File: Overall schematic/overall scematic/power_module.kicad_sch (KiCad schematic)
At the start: 0 parts

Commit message: update kicad
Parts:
- added C1, C3: 10uf, Capacitor_SMD:C_0402_1005Metric, symbol Device:C
- added C4: 4.7uf, Capacitor_SMD:C_0402_1005Metric, symbol Device:C
- added C5: 4.7 uf, Capacitor_SMD:C_0402_1005Metric, symbol Device:C
- added D1: Red LED, LED_SMD:LED_0805_2012Metric, symbol Device:LED
- added D2: Zener Diode, Diode_THT:D_DO-34_SOD68_P2.54mm_Vertical_AnodeUp, symbol Diode:1N47xxA
- added D3: Green LED, Diode_SMD:D_0805_2012Metric, symbol Device:LED
- added J1: USB_B_Micro, Connector_USB:USB_Micro-B_Amphenol_10118194_Horizontal, symbol Connector:USB_B_Micro
- added J2: Battery Charger IC TP4056, SOIC127P600X175-9N, symbol TP4056:TP4056
- added J3, J4, J5, J6: Conn_01x02_Pin, Connector_PinHeader_2.54mm:PinHeader_1x02_P2.54mm_Horizontal, symbol Connector:Conn_01x02_Pin
- added J3_Battery1: Conn_01x02, Connector_Pin:Pin_D1.1mm_L10.2mm_W3.5mm_Flat, symbol Connector_Generic:Conn_01x02
- added Q1, Q2: PMOS, Package_TO_SOT_SMD:SOT-23, symbol Simulation_SPICE:PMOS
- added R1, R2: 1k, Resistor_SMD:R_0402_1005Metric, symbol Device:R
- added R10: 1.6k, Resistor_SMD:R_0201_0603Metric, symbol Device:R
- added R3: 3.6M, Resistor_SMD:R_0402_1005Metric, symbol Device:R
- added R4: 3M, Resistor_SMD:R_0402_1005Metric, symbol Device:R
- added R5: 2.5M, Resistor_SMD:R_0402_1005Metric, symbol Device:R
- added R6: 150k, Resistor_SMD:R_0402_1005Metric, symbol Device:R
- added R7: 1M, Resistor_SMD:R_0402_1005Metric, symbol Device:R
- added R8: 10M, Resistor_SMD:R_0402_1005Metric, symbol Device:R
- added R9: 400m, Resistor_SMD:R_0402_1005Metric, symbol Device:R
- added TP1, TP2, TP3, TP4, TP5: TestPoint, symbol Connector:TestPoint
- added U3: Voltage Regulator LM3670MF, Package_TO_SOT_SMD:TSOT-23-5, symbol Regulator_Switching:LM3670MF
- added U4: LM2902, symbol Amplifier_Operational:LM2902
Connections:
- new net: Q1.2 (G), R7.1
- new net: J5.2 (Pin_2), Q1.3 (S), R3.1, R5.1, U4.4 (V+)
- new net: R3.2, R4.1, U4.2 (-)
- new net: D3.1 (K), R1.1
- new net: J2.7 (~{CHRG}), R1.2
- new net: J2.2 (PROG2), R10.1
- new net: C1.1, J2.5 (BAT), J4.1 (Pin_1), TP2.1
- new net: J2.6 (~{STDBY}), R2.2
- new net: D1.1 (K), R2.1
- new net: D2.2 (A), R6.1, R8.2, U4.11 (V-)
- new net: R7.2, R8.1, U4.1
- new net: D2.1 (K), R5.2, U4.3 (+)
- new net: C4.1, J6.2 (Pin_2), U3.1 (Vin), U3.3 (EN)
- new net Data +: J1.3 (D+)
- new net Data -: J1.2 (D-)
- new net GND: C1.2, C3.2, C4.2, C5.2, J1.5 (GND), J1.6 (Shield), J2.1 (TEMP1), J2.3 (GND_3), J2.4 (VCC4), J3_Battery1.2 (Pin_2), Q2.2 (G), R10.2, R4.2, R6.2, U3.2 (GND)
- new net Supply Voltage: C5.1, TP5.1, U3.4 (FB), U3.5 (SW)
- new net VCC: J3.2 (Pin_2), R9.2
- new net V_Battery: J3_Battery1.1 (Pin_1), J4.2 (Pin_2)
- new net V_RPP: J5.1 (Pin_1), Q2.3 (S), TP3.1
- new net V_UVLO: J6.1 (Pin_1), Q1.1 (D), TP4.1
- new net V_battery: Q2.1 (D)
- new net Vcc_IC: C3.1, D1.2 (A), D3.2 (A), J2.8 (CE), R9.1
- new net Vreg_Out: J1.1 (VBUS), J3.1 (Pin_1), TP1.1
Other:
- note added: "Battery Charger Circuit"
- note added: "Battery Connector"
- note added: "Battery Under-voltage cutout protection"
- note added: "Reverse Polarity Protection"
- note added: "Voltage Regulator 3V3 for Microcontroller"

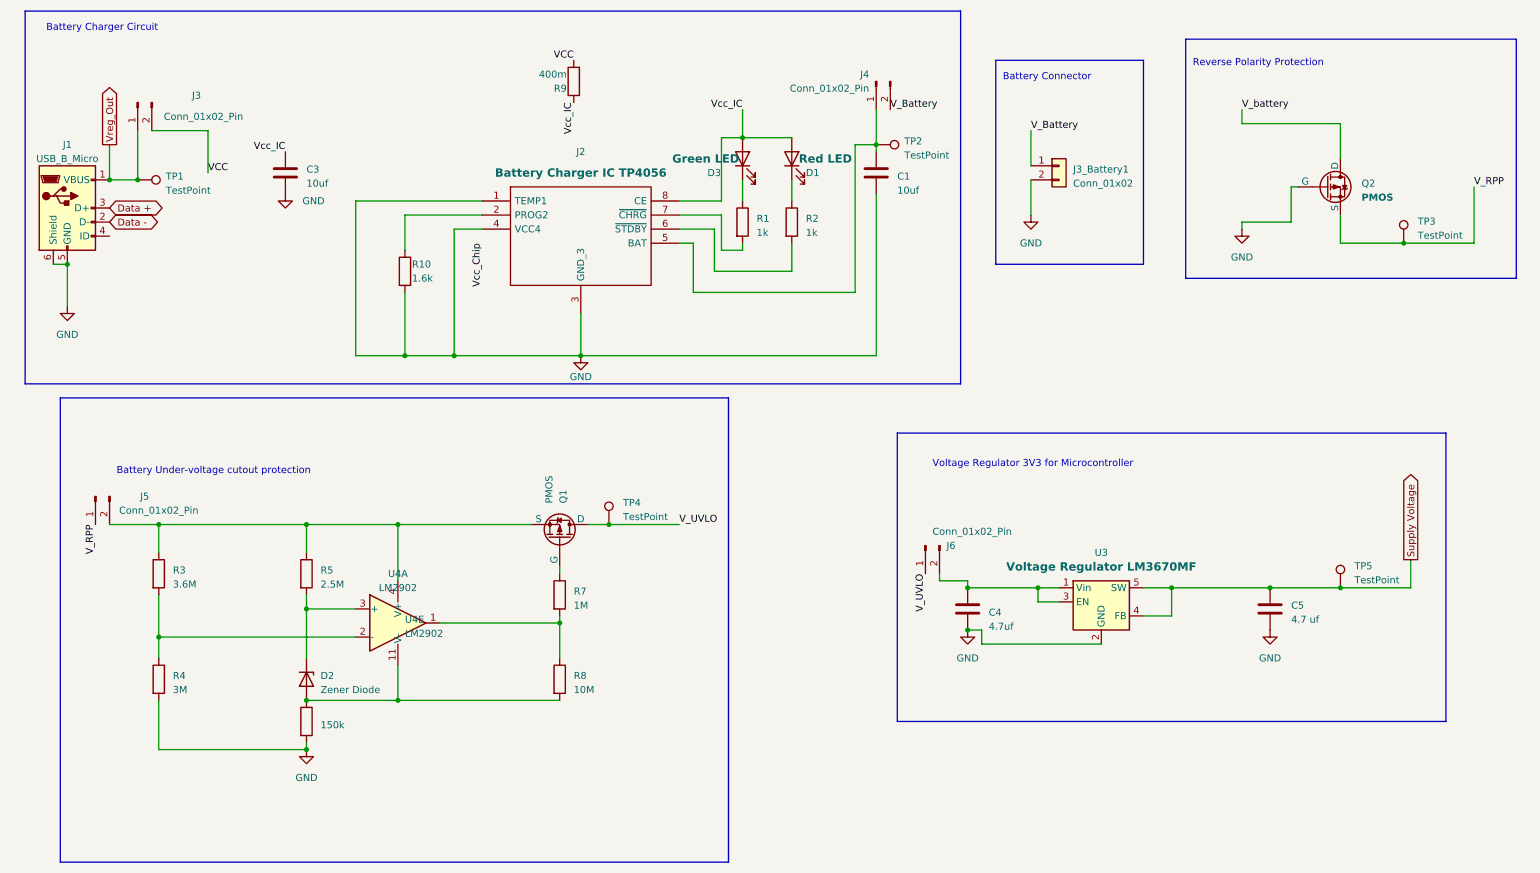
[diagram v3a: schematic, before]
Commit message: updated power sub
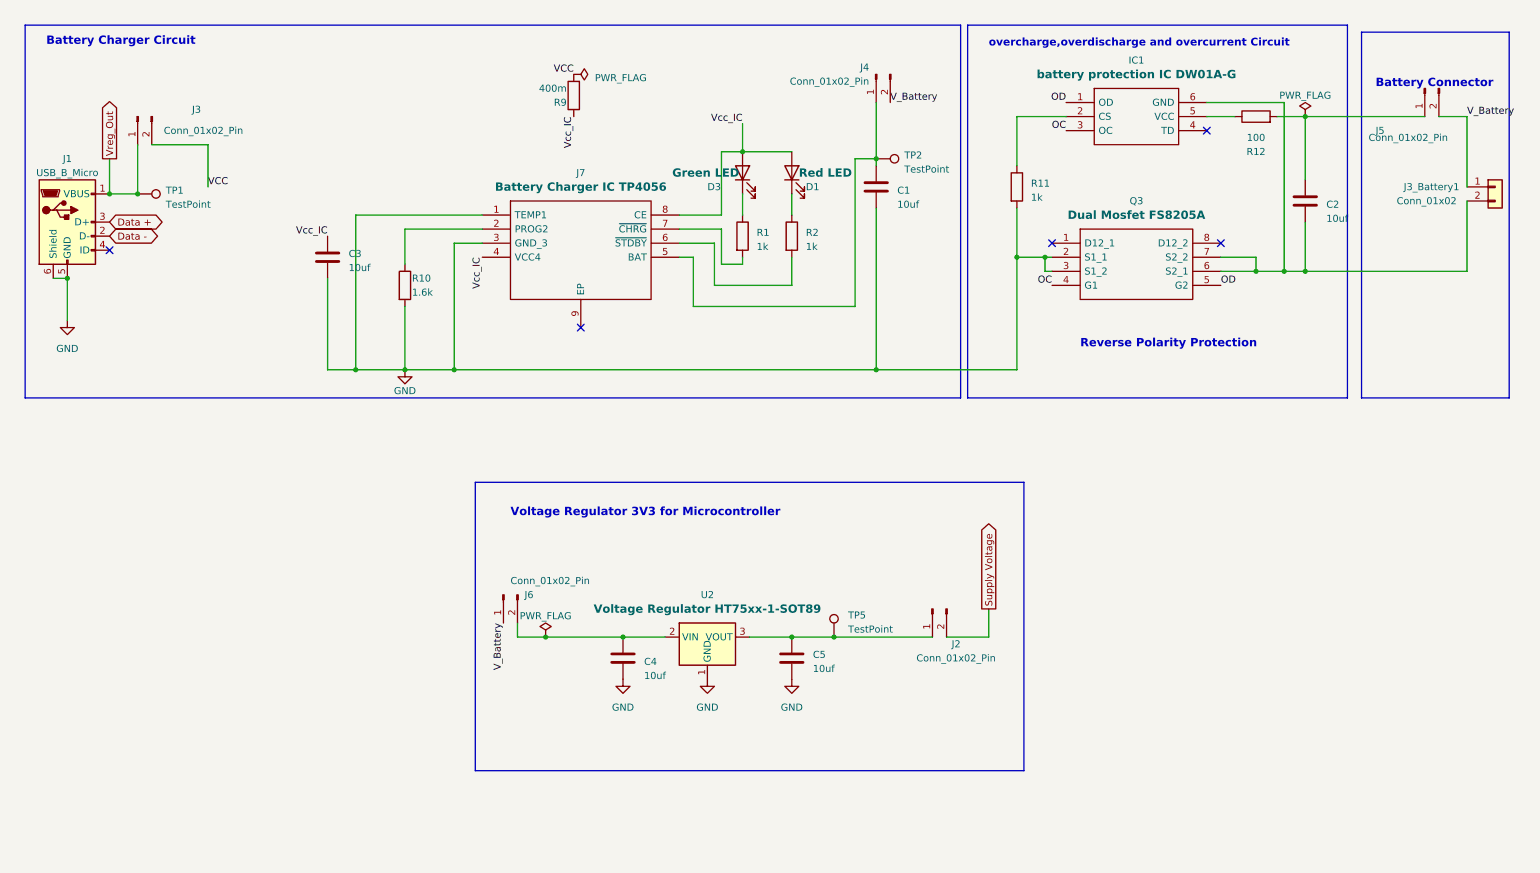
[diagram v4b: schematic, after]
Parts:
- removed D2: Zener Diode, Diode_THT:D_DO-34_SOD68_P2.54mm_Vertical_AnodeUp, symbol Diode:1N47xxA
- removed J2: Battery Charger IC TP4056, SOIC127P600X175-9N, symbol TP4056:TP4056
- removed Q1, Q2: PMOS, Package_TO_SOT_SMD:SOT-23, symbol Simulation_SPICE:PMOS
- removed R3: 3.6M, Resistor_SMD:R_0402_1005Metric, symbol Device:R
- removed R4: 3M, Resistor_SMD:R_0402_1005Metric, symbol Device:R
- removed R5: 2.5M, Resistor_SMD:R_0402_1005Metric, symbol Device:R
- removed R6: 150k, Resistor_SMD:R_0402_1005Metric, symbol Device:R
- removed R7: 1M, Resistor_SMD:R_0402_1005Metric, symbol Device:R
- removed R8: 10M, Resistor_SMD:R_0402_1005Metric, symbol Device:R
- removed TP3, TP4: TestPoint, symbol Connector:TestPoint
- removed U3: Voltage Regulator LM3670MF, Package_TO_SOT_SMD:TSOT-23-5, symbol Regulator_Switching:LM3670MF
- removed U4: LM2902, symbol Amplifier_Operational:LM2902
- added C2: 10uf, Capacitor_SMD:C_0402_1005Metric, symbol Device:C
- added IC1: battery protection IC DW01A-G, SOT95P280X135-6N, symbol DW01A-G:DW01A-G
- added J2: Conn_01x02_Pin, Connector_PinHeader_2.54mm:PinHeader_1x02_P2.54mm_Horizontal, symbol Connector:Conn_01x02_Pin
- added J7: Battery Charger IC TP4056, SOIC127P600X175-9N, symbol TP4056:TP4056
- added Q3: Dual Mosfet FS8205A, SOP65P640X120-8N, symbol FS8205A:FS8205A
- added R11: 1k, Resistor_THT:R_Axial_DIN0207_L6.3mm_D2.5mm_P10.16mm_Horizontal, symbol Device:R
- added R12: 100, Resistor_THT:R_Axial_DIN0207_L6.3mm_D2.5mm_P10.16mm_Horizontal, symbol Device:R
- added U2: Voltage Regulator HT75xx-1-SOT89, Package_TO_SOT_SMD:SOT-89-3, symbol Regulator_Linear:HT75xx-1-SOT89
- C4: value 4.7uf -> 10uf
- C5: value 4.7 uf -> 10uf
- R1, R2: footprint Resistor_SMD:R_0402_1005Metric -> Resistor_THT:R_Axial_DIN0207_L6.3mm_D2.5mm_P10.16mm_Horizontal
- R10: footprint Resistor_SMD:R_0201_0603Metric -> Resistor_THT:R_Axial_DIN0207_L6.3mm_D2.5mm_P10.16mm_Horizontal
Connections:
- net V_UVLO is gone; now on net V_Battery: J6.1 (Pin_1)
- net GND: now also J7.1 (TEMP1), J7.3 (GND_3), Q3.2 (S1_1), Q3.3 (S1_2), R11.2, U2.1 (GND); no longer J3_Battery1.2 (Pin_2)
- net Supply Voltage: now also J2.2 (Pin_2); no longer C5.1, TP5.1
- net V_Battery: now also J5.2 (Pin_2)
- net Vcc_IC: now also J7.4 (VCC4), J7.8 (CE)
- net at R1.2: now also J7.7 (~{CHRG})
- net at R10.1: now also J7.2 (PROG2)
- net at C1.1, J4.1 (Pin_1), TP2.1: now also J7.5 (BAT)
- net at R2.2: now also J7.6 (~{STDBY})
- net at C4.1, J6.2 (Pin_2): now also U2.2 (VIN)
- net V_RPP: no longer names the net of J5.1 (Pin_1)
- net V_RPP: now also C2.1, R12.2
- new net: IC1.5 (VCC), R12.1
- new net: C2.2, IC1.6 (GND), J3_Battery1.2 (Pin_2), Q3.6 (S2_1), Q3.7 (S2_2)
- new net: IC1.2 (CS), R11.1
- new net: C5.1, J2.1 (Pin_1), TP5.1, U2.3 (VOUT)
- new net OC: IC1.3 (OC), Q3.4 (G1)
- new net OD: IC1.1 (OD), Q3.5 (G2)
- no-connect marks 0 -> 5
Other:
- note added: "overcharge,overdischarge and overcurrent Circuit"
- note removed: "Battery Under-voltage cutout protection"

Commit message: fully annotated
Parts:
- removed J3_Battery1: Conn_01x02, Connector_Pin:Pin_D1.1mm_L10.2mm_W3.5mm_Flat, symbol Connector_Generic:Conn_01x02
- added JP1, JP2: Jumper_2_Bridged, symbol Jumper:Jumper_2_Bridged
- IC1: footprint SOT95P280X135-6N -> (none)
- J7: footprint SOIC127P600X175-9N -> (none)
- Q3: footprint SOP65P640X120-8N -> (none)
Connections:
- net V_Battery: now also JP1.1 (A); no longer J4.2 (Pin_2), J6.1 (Pin_1)
- net at C2.2, IC1.6 (GND), Q3.6 (S2_1)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: now also JP2.2 (B)
- net Supply Voltage renamed Supply_Voltage
- new net Battery+: J4.2 (Pin_2), J6.1 (Pin_1), JP1.2 (B)
- new net Battery-: JP2.1 (A)
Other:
- moved on the sheet: C1, C2, C3, C4, C5, D1, D3, IC1, J1, J2, J3, J4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

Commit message: updated everything
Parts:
- removed J5: Conn_01x02_Pin, Connector_PinHeader_2.54mm:PinHeader_1x02_P2.54mm_Horizontal, symbol Connector:Conn_01x02_Pin
- removed JP1, JP2: Jumper_2_Bridged, symbol Jumper:Jumper_2_Bridged
- added J10, J11: Conn_01x02_Pin, Connector_PinHeader_2.54mm:PinHeader_1x02_P2.54mm_Vertical, symbol Connector:Conn_01x02_Pin
- IC1: footprint (none) -> DW01A:SOT95P280X135-6N
- J7: footprint (none) -> TP4056:SOIC127P600X175-9N
- Q3: footprint (none) -> FB8205A:SOP65P640X120-8N
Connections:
- net Battery+: now also J10.2 (Pin_2)
- net Battery-: now also J11.1 (Pin_1)
- net VCC: no longer R9.2
- net at C2.1, R12.2: now also J10.1 (Pin_1)
- net at C2.2, IC1.6 (GND), Q3.6 (S2_1)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: now also J11.2 (Pin_2)
- net Vreg_Out: no longer names the net of J1.1 (VBUS), J3.1 (Pin_1), TP1.1
- new net +5V: R9.2
- no-connect marks 5 -> 7

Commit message: BOM
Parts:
- J2, J3, J4, J6: footprint Connector_PinHeader_2.54mm:PinHeader_1x02_P2.54mm_Horizontal -> Connector_PinHeader_2.54mm:PinHeader_1x02_P2.54mm_Vertical
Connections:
- net VCC is gone; now on net Battery+: J3.2 (Pin_2)
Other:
- company: (none) -> University of capetown
- title: (none) -> 3088_group22_design
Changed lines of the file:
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@@
 (kicad_sch (version 20230121) (generator eeschema)
   (paper "A4")
+  (title_block
+    (title "3088_group22_design")
+    (date "2023-03-20")
+    (rev "3")
+    (company "University of capetown")
+  )
   (junction (at 166.37 85.09) (diameter 0) (color 0 0 0 0)
   )
@@
     (effects (font (size 1.27 1.27)) (justify right bottom))
   )
-  (label "VCC" (at 45.72 52.07 0) (fields_autoplaced)
-    (effects (font (size 1.27 1.27)) (justify left bottom))
-  )
   (label "OC" (at 200.66 41.91 180) (fields_autoplaced)
     (effects (font (size 1.27 1.27)) (justify right bottom))
@@
   )
   (hierarchical_label "Battery+" (shape bidirectional) (at 273.05 50.8 0) (fields_autoplaced)
+    (effects (font (size 1.27 1.27)) (justify left))
+  )
+  (hierarchical_label "Battery+" (shape bidirectional) (at 45.72 52.07 0) (fields_autoplaced)
     (effects (font (size 1.27 1.27)) (justify left))
   )
@@
       (effects (font (size 1.27 1.27)) (justify left))
     )
-    (property "Footprint" "Connector_PinHeader_2.54mm:PinHeader_1x02_P2.54mm_Horizontal" (at 33.02 39.37 0)
+    (property "Footprint" "Connector_PinHeader_2.54mm:PinHeader_1x02_P2.54mm_Vertical" (at 33.02 39.37 0)
       (effects (font (size 1.27 1.27)) hide)
     )
@@
       (effects (font (size 1.27 1.27)) (justify right))
     )
-    (property "Footprint" "Connector_PinHeader_2.54mm:PinHeader_1x02_P2.54mm_Horizontal" (at 99.06 125.73 0)
+    (property "Footprint" "Connector_PinHeader_2.54mm:PinHeader_1x02_P2.54mm_Vertical" (at 99.06 125.73 0)
       (effects (font (size 1.27 1.27)) hide)
     )
@@
       (effects (font (size 1.27 1.27)) (justify left))
     )
-    (property "Footprint" "Connector_PinHeader_2.54mm:PinHeader_1x02_P2.54mm_Horizontal" (at 176.53 128.27 0)
+    (property "Footprint" "Connector_PinHeader_2.54mm:PinHeader_1x02_P2.54mm_Vertical" (at 176.53 128.27 0)
       (effects (font (size 1.27 1.27)) hide)
     )
@@
       (effects (font (size 1.27 1.27)) (justify left))
     )
-    (property "Footprint" "Connector_PinHeader_2.54mm:PinHeader_1x02_P2.54mm_Horizontal" (at 166.37 31.75 0)
-      (effects (font (size 1.27 1.27)) hide)
-    )
+    (property "Footprint" "Connector_PinHeader_2.54mm:PinHeader_1x02_P2.54mm_Vertical" (at 166.37 31.75 0)
+      (effects (font (size 1.27 1.27)) hide)
+    )

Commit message: The final Gerber
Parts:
- removed J10, J11: Conn_01x02_Pin, Connector_PinHeader_2.54mm:PinHeader_1x02_P2.54mm_Vertical, symbol Connector:Conn_01x02_Pin
- added J5: Conn_01x02_Pin, Connector_PinHeader_2.54mm:PinHeader_1x02_P2.54mm_Vertical, symbol Connector:Conn_01x02_Pin
- added JP1, JP2: Jumper_2_Bridged, Jumper:SolderJumper-2_P1.3mm_Bridged2Bar_Pad1.0x1.5mm, symbol Jumper:Jumper_2_Bridged
- C1, C2, C3, C4, C5: value 10uf -> C
- D1: value Red LED -> LED
- D3: value Green LED -> LED
- IC1: value battery protection IC DW01A-G -> DW01A-G; footprint DW01A:SOT95P280X135-6N -> BAT60JFILM:DW01A
- J7: value Battery Charger IC TP4056 -> TP4056; footprint TP4056:SOIC127P600X175-9N -> BAT60JFILM:TP4056
- Q3: value Dual Mosfet FS8205A -> FS8205A; footprint FB8205A:SOP65P640X120-8N -> BAT60JFILM:FB8205A
- R1, R11, R2: value 1k -> R
- R10: value 1.6k -> R
- R12: value 100 -> R
- R9: value 400m -> R
- U2: value Voltage Regulator HT75xx-1-SOT89 -> HT75xx-1-SOT89
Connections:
- net Battery+: now also JP1.2 (B); no longer J3.2 (Pin_2)
- net Battery-: now also JP2.1 (A)
- net at C2.1, R12.2: now also J5.1 (Pin_1)
- net Vreg_Out: now reaches J1.1 (VBUS), J3.1 (Pin_1), TP1.1
- net at C2.2, IC1.6 (GND), Q3.6 (S2_1)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: now also JP2.2 (B)
- net +5V renamed VCC
- net VCC: now also J3.2 (Pin_2)
- new net V_Battery: J5.2 (Pin_2), JP1.1 (A)
- no-connect marks 7 -> 5
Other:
- company: University of capetown -> (none)
- title: 3088_group22_design -> (none)
